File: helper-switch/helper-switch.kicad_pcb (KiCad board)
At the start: 2 copper layers, 15 x 25.2 mm, 7 parts, among them J1 +5V_IN, J2 +5V_OUT, J3 +12V_IN, J4 +12V_OUT, J5 -12V_IN, J6 -12V_OUT, SW1 POWER

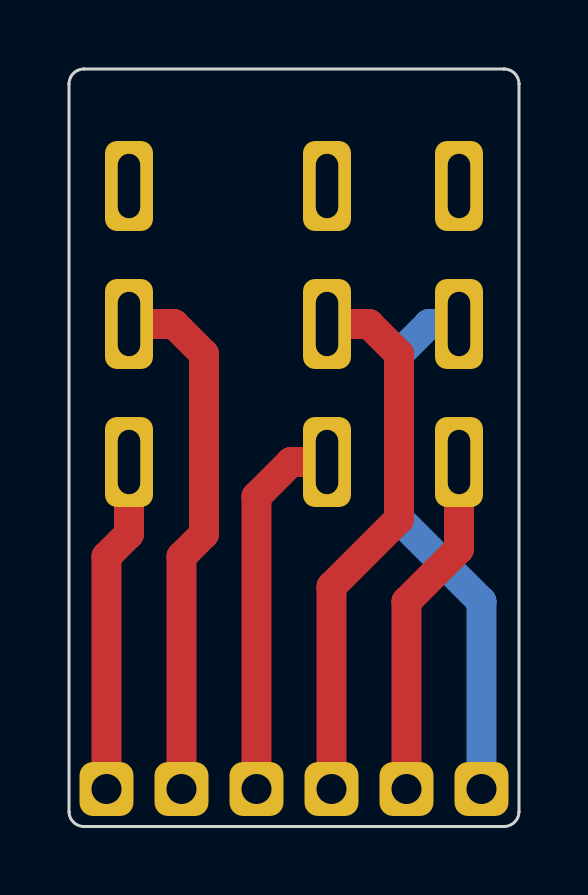
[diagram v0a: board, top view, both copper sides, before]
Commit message: Add markings to switch and jack helpers
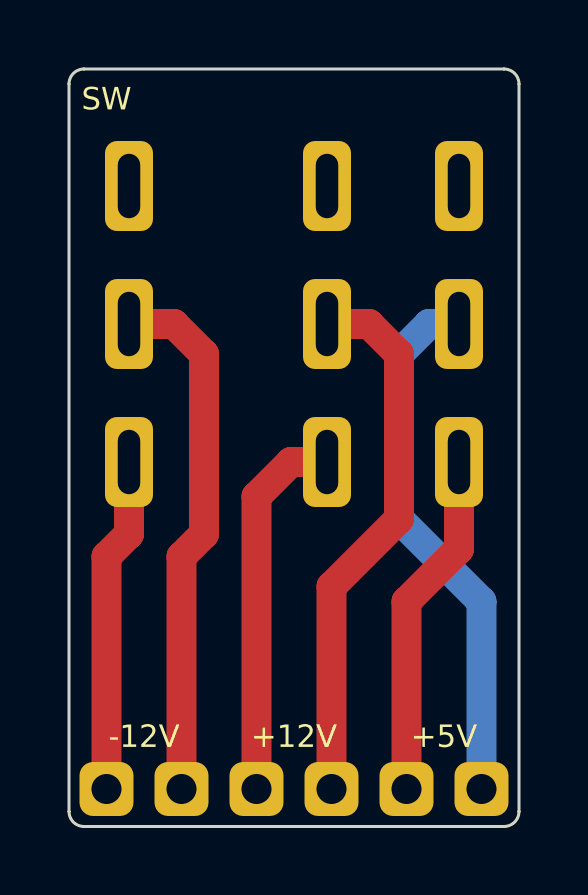
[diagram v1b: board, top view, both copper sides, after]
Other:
- board text added: "+12V"
- board text added: "+5V"
- board text added: "-12V"
- board text added: "SW"
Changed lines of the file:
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@@
       (layerselection 0x00010f0_ffffffff)
       (disableapertmacros false)
-      (usegerberextensions false)
+      (usegerberextensions true)
       (usegerberattributes true)
       (usegerberadvancedattributes true)
@@
   (gr_line (start 23 21.5) (end 37 21.5) (layer "Edge.Cuts") (width 0.1))
   (gr_arc (start 37.5 46.25) (mid 37.353553 46.603553) (end 37 46.75) (layer "Edge.Cuts") (width 0.1))
+  (gr_text "SW" (at 23.75 22.5) (layer "F.SilkS")
+    (effects (font (size 0.75 0.75) (thickness 0.12)))
+  )
+  (gr_text "-12V" (at 25 43.75) (layer "F.SilkS")
+    (effects (font (size 0.75 0.75) (thickness 0.15)))
+  )
+  (gr_text "+5V" (at 35 43.75) (layer "F.SilkS")
+    (effects (font (size 0.75 0.75) (thickness 0.15)))
+  )
+  (gr_text "+12V" (at 30 43.75) (layer "F.SilkS")
+    (effects (font (size 0.75 0.75) (thickness 0.15)))
+  )
   (segment (start 36.25 39.25) (end 33.5 36.5) (width 1) (layer "B.Cu") (net 1))
   (segment (start 34.5 30) (end 35.5 30) (width 1) (layer "B.Cu") (net 1))

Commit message: Update helper switch to KiCad 7, Adjust markings
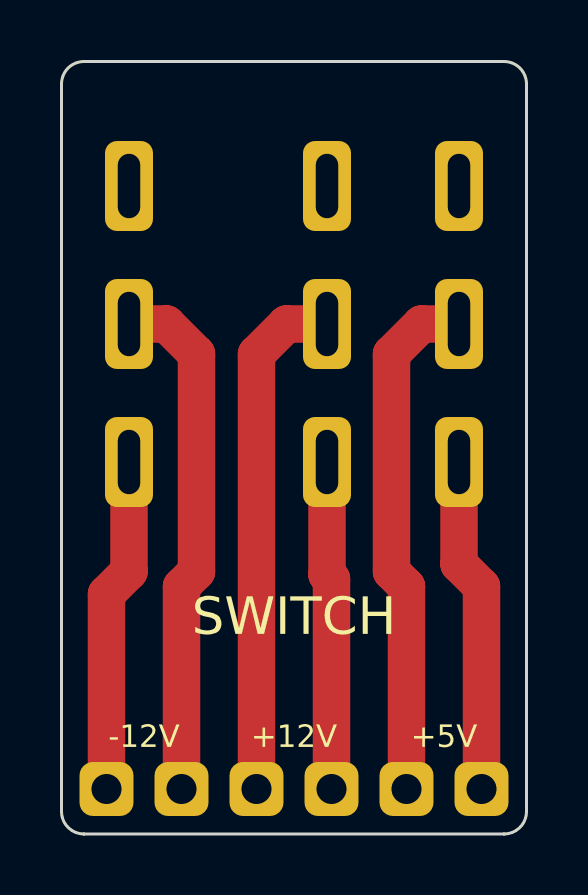
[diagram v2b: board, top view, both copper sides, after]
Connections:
- SW1 pad 2: /+5V_IN -> /+5V_OUT
- SW1 pad 3: /+5V_OUT -> /+5V_IN
- SW1 pad 5: /+12V_IN -> /+12V_OUT
- SW1 pad 6: /+12V_OUT -> /+12V_IN
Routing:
- net /+12V_IN: track 18.2 -> 11.0 mm
- net /+5V_IN: track 18.1 -> 11.2 mm
- net /+5V_OUT: track 11.6 -> 17.4 mm
- net /+12V_OUT: track 12.6 -> 17.3 mm
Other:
- board size 15 x 25.2 mm -> 15.5 x 25.8 mm
- board text added: "SWITCH"
- board text removed: "SW"
